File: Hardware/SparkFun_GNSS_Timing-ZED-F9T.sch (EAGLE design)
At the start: 68 parts, among them J1 Radio, J2 Qwiic Right Angle, J3 PTH, J4 Qwiic Right Angle, J5 USB Female Type C Connector, U3 U-BLOX_ZED_F9T, U5 AP2112K-3.3V

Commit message: Change RF trace width and other small changes from design review.
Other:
- note added: "Polygon Isolation: 8mil/0.2032mm"
- note added: "RF Trace Width: 13.74mil/0.349mm"
- note added: "v10"
- note removed: "Polygon Isolation: 6mil/0.1524mm"
- note removed: "RF Trace Width: 13mil/0.33mm"
- note removed: "v11"
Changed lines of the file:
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@@
 <class number="2" name="3.3V" width="0.508" drill="0.3048">
 </class>
-<class number="3" name="RF" width="0.33" drill="0">
+<class number="3" name="RF" width="0.349" drill="0">
 <clearance class="3" value="0.2032"/>
 </class>
@@
 <sheet>
 <plain>
-<text x="420.624" y="7.366" size="2.54" layer="94">v11</text>
+<text x="420.624" y="7.366" size="2.54" layer="94">v10</text>
 <text x="114.3" y="187.96" size="1.778" layer="97" align="center">7-bit unshifted I2C address: 0x42</text>
 <text x="115.062" y="262.382" size="2.54" layer="94" rot="MR180" align="center">u-blox ZED-F9T</text>
@@
 <text x="30.48" y="259.08" size="1.27" layer="97">Er: 4.6</text>
 <text x="30.48" y="266.7" size="1.27" layer="97">Copper Thickness (1oz): 1.4mil/0.035mm</text>
-<text x="30.48" y="254" size="1.27" layer="97">RF Trace Width: 13mil/0.33mm</text>
-<text x="30.48" y="256.54" size="1.27" layer="97">Polygon Isolation: 6mil/0.1524mm</text>
+<text x="30.48" y="254" size="1.27" layer="97">RF Trace Width: 13.74mil/0.349mm</text>
+<text x="30.48" y="256.54" size="1.27" layer="97">Polygon Isolation: 8mil/0.2032mm</text>
 <text x="406.4" y="55.88" size="1.27" layer="97">No clean process</text>
 <text x="30.48" y="261.62" size="1.27" layer="97">Dielectric thickness (layer 1 to 2): 0.2mm</text>

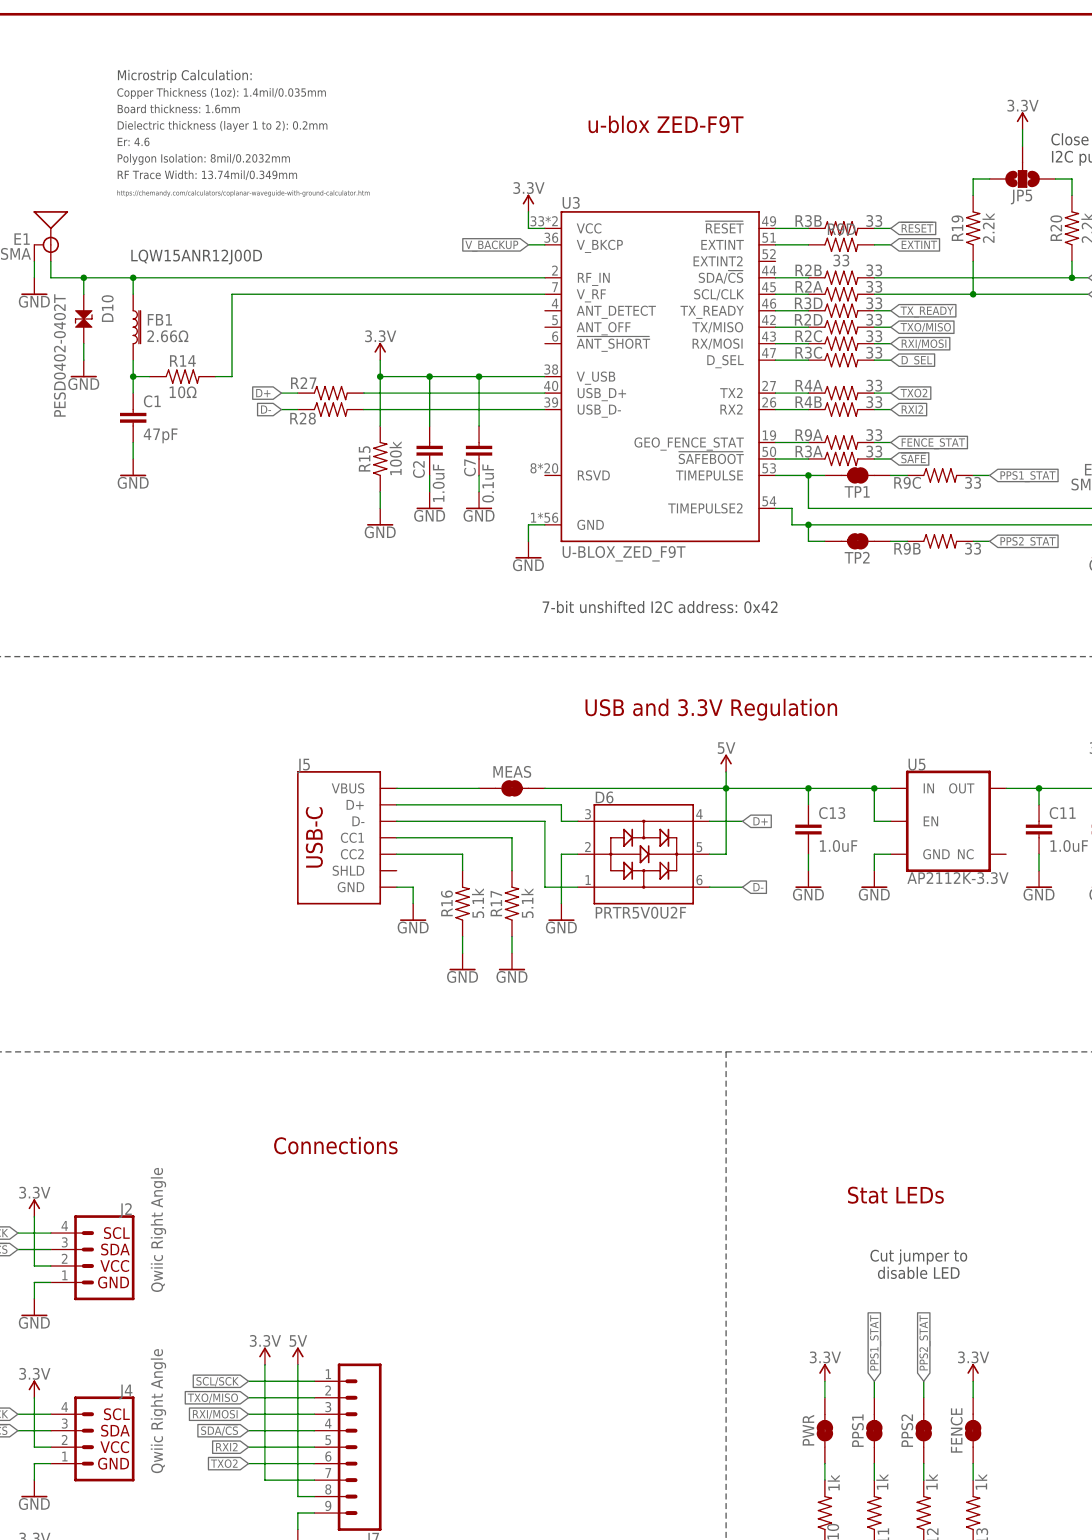
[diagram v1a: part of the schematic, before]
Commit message: Add production panel.
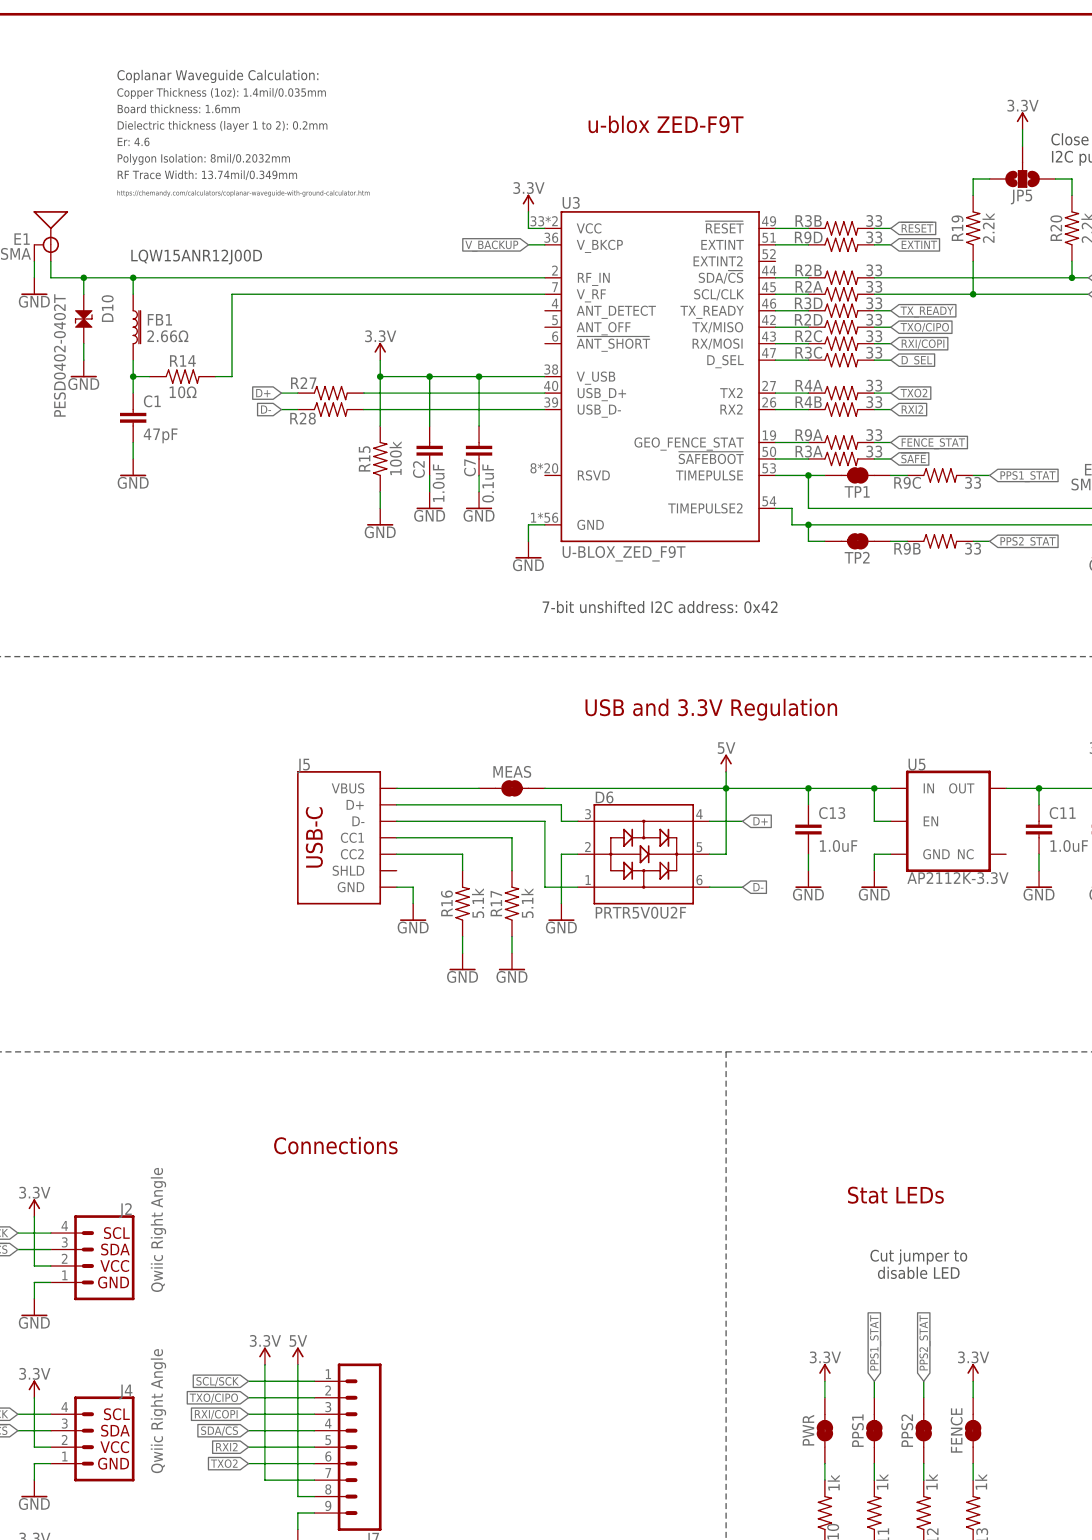
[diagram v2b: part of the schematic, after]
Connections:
- net RXI/MOSI renamed RXI/COPI
- net TXO/MISO renamed TXO/CIPO
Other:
- note added: "Coplanar Waveguide Calculation:"
- note removed: "Microstrip Calculation:"
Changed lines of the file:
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@@
 <text x="30.48" y="261.62" size="1.27" layer="97">Dielectric thickness (layer 1 to 2): 0.2mm</text>
 <text x="30.48" y="251.46" size="0.762" layer="97">https://chemandy.com/calculators/coplanar-waveguide-with-ground-calculator.htm</text>
-<text x="30.48" y="269.24" size="1.524" layer="97" ratio="15">Microstrip Calculation:</text>
+<text x="30.48" y="269.24" size="1.524" layer="97" ratio="15">Coplanar Waveguide Calculation:</text>
 <wire x1="0" y1="119.38" x2="124.46" y2="119.38" width="0.2032" layer="97" style="longdash"/>
 <wire x1="124.46" y1="119.38" x2="124.46" y2="0" width="0.2032" layer="97" style="longdash"/>
@@
 </instance>
 <instance part="R9" gate="D" x="142.24" y="243.84" smashed="yes">
-<attribute name="NAME" x="142.24" y="245.364" size="1.778" layer="95" font="vector" align="bottom-center"/>
-<attribute name="VALUE" x="142.24" y="242.316" size="1.778" layer="96" font="vector" align="top-center"/>
+<attribute name="NAME" x="137.16" y="244.094" size="1.778" layer="95" font="vector" align="bottom-center"/>
+<attribute name="VALUE" x="147.32" y="244.094" size="1.778" layer="96" font="vector" rot="R180" align="top-center"/>
 </instance>
 <instance part="R9" gate="A" x="142.24" y="213.36" smashed="yes">
@@
 </segment>
 </net>
-<net name="RXI/MOSI" class="0">
+<net name="RXI/COPI" class="0">
 <segment>
 <wire x1="60.96" y1="63.5" x2="50.8" y2="63.5" width="0.1524" layer="91"/>
@@
 </segment>
 </net>
-<net name="TXO/MISO" class="0">
+<net name="TXO/CIPO" class="0">
 <segment>
 <wire x1="60.96" y1="66.04" x2="50.8" y2="66.04" width="0.1524" layer="91"/>
